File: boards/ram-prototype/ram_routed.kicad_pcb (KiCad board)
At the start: 4 copper layers, 173 x 118 mm, 611 parts, among them J1 PinHeader_1x24_P2\.54mm_Verti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, J2 PinHeader_1x04_P2\.54mm_Verti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, J3 PinHeader_1x14_P2\.54mm_Verti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, J4 PinHeader_2x08_P2\.54mm_Verti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, U1 DSBGA\-5_NumericPads, U10 DSBGA\-5_NumericPads, U100 DSBGA\-5_NumericPads, U101 DSBGA\-5_NumericPads, U102 DSBGA\-5_NumericPads, U103 DSBGA\-5_NumericPads, U104 DSBGA\-5_NumericPads, U105 DSBGA\-5_NumericPads, U106 DSBGA\-5_NumericPads, U107 DSBGA\-5_NumericPads, U108 DSBGA\-5_NumericPads, U109 DSBGA\-5_NumericPads, U11 DSBGA\-5_NumericPads, U110 DSBGA\-5_NumericPads, U111 DSBGA\-5_NumericPads, U112 DSBGA\-5_NumericPads, U113 DSBGA\-5_NumericPads, U114 DSBGA\-5_NumericPads, U115 DSBGA\-5_NumericPads, U116 DSBGA\-5_NumericPads, U117 DSBGA\-5_NumericPads, U118 DSBGA\-5_NumericPads, U119 DSBGA\-5_NumericPads, U12 DSBGA\-5_NumericPads, U120 DSBGA\-5_NumericPads, U121 DSBGA\-5_NumericPads, U122 DSBGA\-5_NumericPads, U123 DSBGA\-5_NumericPads, U124 DSBGA\-5_NumericPads, U125 DSBGA\-5_NumericPads, U126 DSBGA\-5_NumericPads, U127 DSBGA\-5_NumericPads, U128 DSBGA\-5_NumericPads, U129 DSBGA\-5_NumericPads, U13 DSBGA\-5_NumericPads, U130 DSBGA\-5_NumericPads, U131 DSBGA\-5_NumericPads, U132 DSBGA\-5_NumericPads, U133 DSBGA\-5_NumericPads, U134 DSBGA\-5_NumericPads, U135 DSBGA\-5_NumericPads, U136 DSBGA\-5_NumericPads, U137 DSBGA\-5_NumericPads, U138 DSBGA\-5_NumericPads, U139 DSBGA\-5_NumericPads, U14 DSBGA\-5_NumericPads, U140 DSBGA\-5_NumericPads, U141 DSBGA\-5_NumericPads, U142 DSBGA\-5_NumericPads, U143 DSBGA\-5_NumericPads, U144 DSBGA\-5_NumericPads, U145 DSBGA\-5_NumericPads, U146 DSBGA\-5_NumericPads, U147 DSBGA\-5_NumericPads, U148 DSBGA\-5_NumericPads, U149 DSBGA\-5_NumericPads, U15 DSBGA\-5_NumericPads, U150 DSBGA\-5_NumericPads, U151 DSBGA\-5_NumericPads, U152 DSBGA\-5_NumericPads, U153 DSBGA\-5_NumericPads, U154 DSBGA\-5_NumericPads, U155 DSBGA\-5_NumericPads, U156 DSBGA\-5_NumericPads, U157 DSBGA\-5_NumericPads, U158 DSBGA\-5_NumericPads, U159 DSBGA\-5_NumericPads, U16 DSBGA\-5_NumericPads, U160 DSBGA\-5_NumericPads, U161 DSBGA\-5_NumericPads, U162 DSBGA\-5_NumericPads, U163 DSBGA\-5_NumericPads, U164 DSBGA\-5_NumericPads, U165 DSBGA\-5_NumericPads, U166 DSBGA\-5_NumericPads, U167 DSBGA\-5_NumericPads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

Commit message: fix NAND LED anode route, COL_SEL trunk gap, and pad index precision
- Fix CLK LED approach route: T-branch from clk_pos[0] instead of
  clk_via_x (0.05mm gap caused dangling cleanup to delete LED route)
- Fix COL_SEL trunk extension: use actual bottom pin Y from
  get_pad_position() instead of hardcoded crtyd_bot_y (0.55mm gap)
- Increase _build_net_pad_index precision to 3 decimals to match
  get_pad_position/add_trace precision
- Save raw post-SES-import PCB to verify_output/ for inspection
- Post-routing: 36 errors -> 3 (1 nCE unconnected + 2 solder mask)

Co-Authored-By: Claude Opus 4.6 (1M context) <noreply@anthropic.com>
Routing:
- net /Address Decoder/nA2: track 50.0 -> 35.6 mm, vias 2 -> 3
- net /Column Select/GB3: track 43.6 -> 57.1 mm, vias 3 -> 2
- net /Address Decoder/A1: track 76.5 -> 63.7 mm, vias 2 -> 3
- net /COL_SEL_2: track 93.0 -> 101.9 mm, vias 1 -> 2
- net /COL_SEL_7: track 67.8 -> 59.6 mm, vias 2 -> 0
- net /Address Decoder/G3: track 37.0 -> 45.0 mm, vias 3 -> 2
- net /COL_SEL_8: track 62.1 -> 54.6 mm, vias 1 -> 0
- net /Address Decoder/A0: track 80.4 -> 73.2 mm, vias 5 -> 3
- net /COL_SEL_4: track 87.4 -> 94.2 mm, vias 2 -> 1
- net /Address Decoder/G1: track 28.3 -> 35.1 mm
- net /Column Select/GA1: track 66.1 -> 72.6 mm, vias 6 -> 7
- net /Address Decoder/DEC3_0: track 23.4 -> 29.7 mm
- net /DEC3_7: track 79.9 -> 86.2 mm, vias 1 -> 2
- net /COL_SEL_9: track 55.7 -> 49.5 mm, vias 2 -> 0
- net /COL_SEL_3: track 87.5 -> 93.6 mm, vias 1 -> 2
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
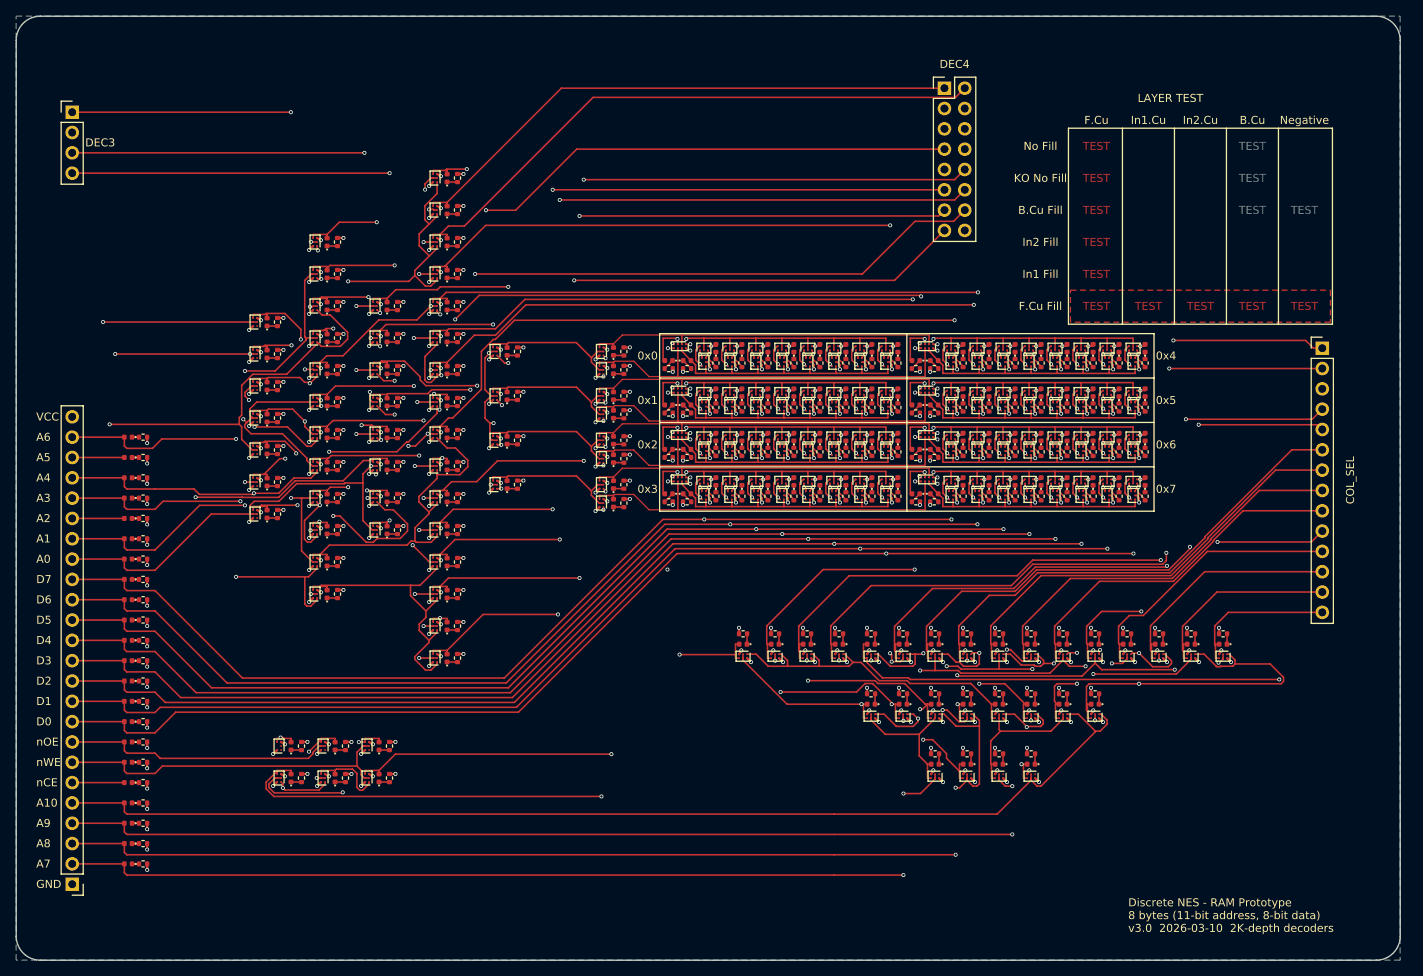
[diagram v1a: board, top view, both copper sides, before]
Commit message: reorder connector control pins to nCE/nOE/nWE top-to-bottom
Move nCE to pin 8 (top), nOE to pin 7, nWE to pin 6 (bottom) on the
24-pin connector. Previous order was nCE/nWE/nOE which put nCE at the
bottom, making it harder for the autorouter to reach control_logic.

Post-routing: 3 errors (2 solder mask bridge), 3 warnings. The nCE
unconnected error from the previous run is eliminated.

Co-Authored-By: Claude Opus 4.6 (1M context) <noreply@anthropic.com>
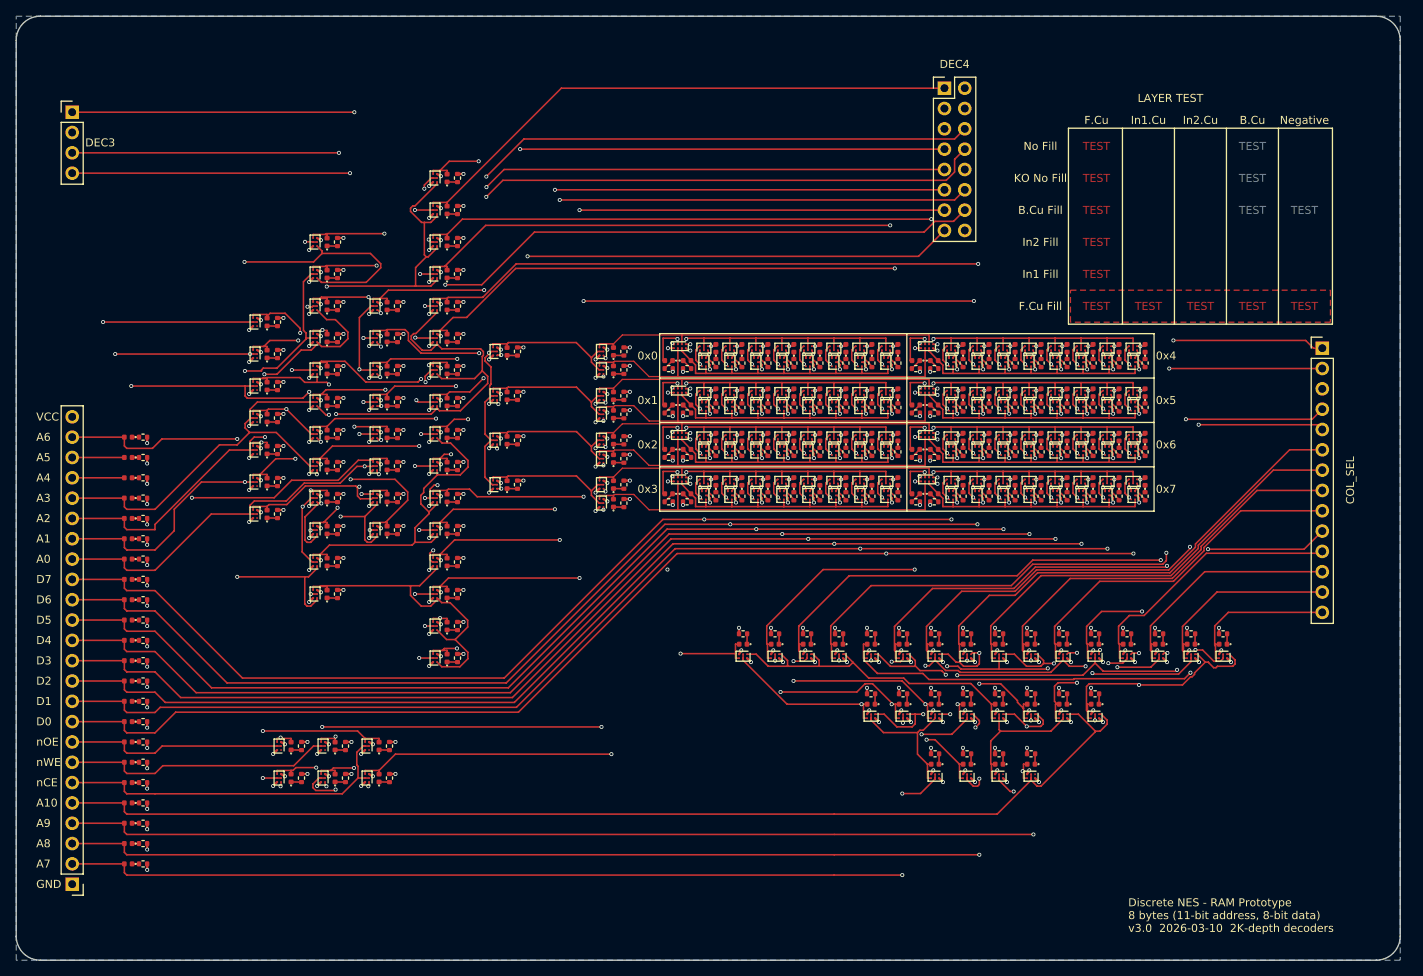
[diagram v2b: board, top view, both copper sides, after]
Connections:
- D16 pad 2: /nOE -> /nCE
- D17 pad 2: /nWE -> /nOE
- D18 pad 2: /nCE -> /nWE
- J1 pad 6: /nCE -> /nWE
- J1 pad 7: /nWE -> /nOE
- J1 pad 8: /nOE -> /nCE
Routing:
- net /nCE: track 6.52 -> 27.7 mm
- net /Address Decoder/nA2: track 35.6 -> 54.7 mm, vias 3 -> 2
- net /Column Select/GB3: track 57.1 -> 39.1 mm, vias 2 -> 3
- net /Address Decoder/HB1: track 50.5 -> 64.4 mm, vias 5 -> 2
- net /WRITE_ACTIVE: track 102.5 -> 92.4 mm, vias 5 -> 7
- net /Address Decoder/A2: track 67.9 -> 58.6 mm, vias 1 -> 2
- net /COL_SEL_4: track 94.2 -> 87.4 mm
- net /Address Decoder/G1: track 35.1 -> 28.4 mm
- net /DEC4_2: track 75.8 -> 82.5 mm, vias 0 -> 1
- net /Address Decoder/A3: track 57.1 -> 50.5 mm, vias 2 -> 0
- net /Column Select/GA3: track 70.8 -> 64.3 mm
- net /Address Decoder/G3: track 45.0 -> 38.5 mm
- net /Address Decoder/nA0: track 53.0 -> 47.5 mm, vias 5 -> 3
- net Net-(D188-A): track 9.51 -> 14.9 mm
- net /DEC3_4: track 74.3 -> 79.6 mm
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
